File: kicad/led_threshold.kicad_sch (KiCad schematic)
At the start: 14 parts, among them U16 PC817, U19 PC817, U21 OPA189

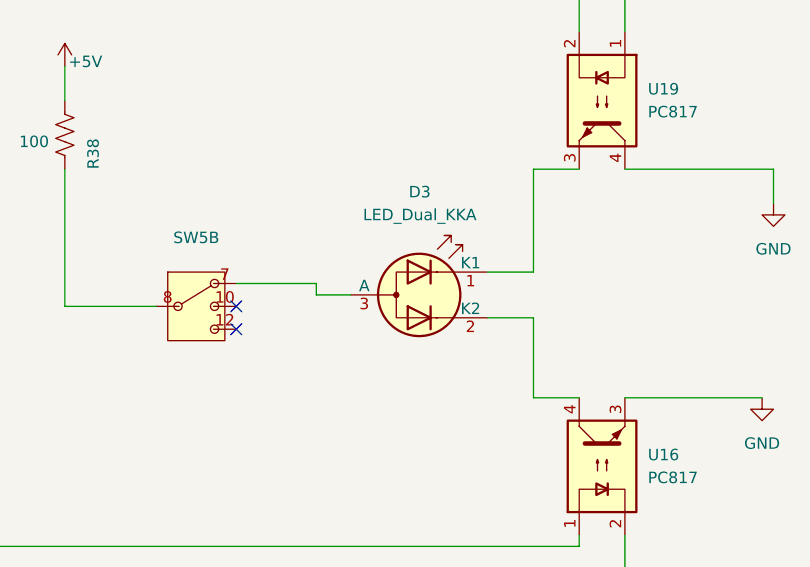
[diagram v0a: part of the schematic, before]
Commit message: Finished Schematic and Assigning Footprint pending Review, TODO: Layout Board
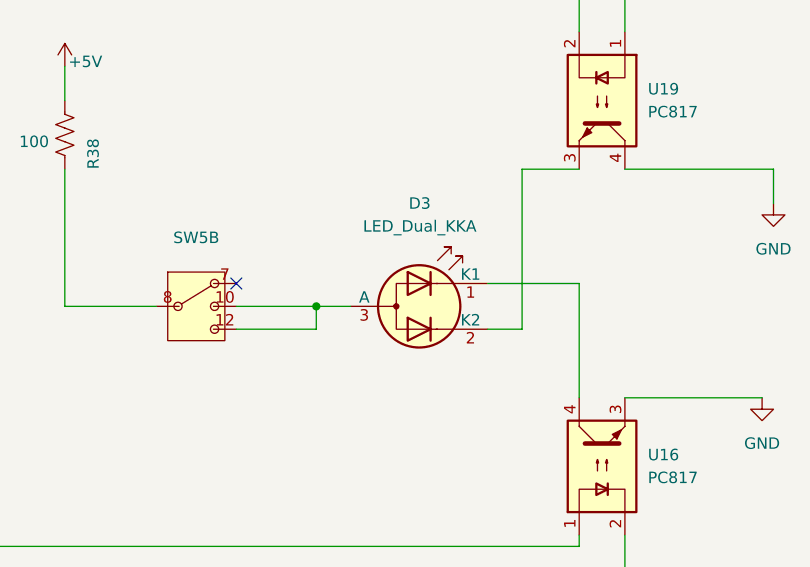
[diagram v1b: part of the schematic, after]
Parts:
- SW5: DIGIKEY (none) -> EG6100-ND; PARTNO (none) -> 1004P6T1B4M7RE
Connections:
- net at U19.3: now also D3.2 (K2); no longer D3.1 (K1)
- net at U16.4: now also D3.1 (K1); no longer D3.2 (K2)
- net at SW5.10: now also D3.3 (A), SW5.12
- net at SW5.7: no longer D3.3 (A)
- no-connect marks 4 -> 3
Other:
- moved on the sheet: D3
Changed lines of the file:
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@@
 	)
 	(junction
+		(at 194.31 66.04)
+		(diameter 0)
+		(color 0 0 0 0)
+	)
+	(junction
 		(at 132.08 116.84)
 		(diameter 0)
@@
 	)
 	(no_connect
-		(at 185.42 66.04)
-	)
-	(no_connect
-		(at 185.42 68.58)
+		(at 185.42 63.5)
 	)
 	(no_connect
@@
 	(wire
 		(pts
+			(xy 213.36 63.5) (xy 223.52 63.5)
+		)
+		(stroke
+			(width 0)
+			(type default)
+		)
+	)
+	(wire
+		(pts
 			(xy 166.37 66.04) (xy 176.53 66.04)
 		)
@@
 	(wire
 		(pts
-			(xy 137.16 105.41) (xy 137.16 106.68)
+			(xy 217.17 50.8) (xy 223.52 50.8)
 		)
 		(stroke
@@
 	(wire
 		(pts
-			(xy 115.57 22.86) (xy 115.57 24.13)
+			(xy 137.16 105.41) (xy 137.16 106.68)
 		)
 		(stroke
@@
 	(wire
 		(pts
-			(xy 93.98 82.55) (xy 87.63 82.55)
+			(xy 115.57 22.86) (xy 115.57 24.13)
 		)
 		(stroke
@@
 	(wire
 		(pts
-			(xy 228.6 19.05) (xy 228.6 17.78)
+			(xy 93.98 82.55) (xy 87.63 82.55)
 		)
 		(stroke
@@
 	(wire
 		(pts
-			(xy 218.44 67.31) (xy 218.44 76.2)
+			(xy 228.6 19.05) (xy 228.6 17.78)
 		)
 		(stroke
@@
 	(wire
 		(pts
-			(xy 44.45 62.23) (xy 44.45 76.2)
+			(xy 194.31 68.58) (xy 194.31 66.04)
 		)
 		(stroke
@@
 	(wire
 		(pts
-			(xy 228.6 26.67) (xy 228.6 35.56)
+			(xy 44.45 62.23) (xy 44.45 76.2)
 		)
 		(stroke
@@
 	(wire
 		(pts
-			(xy 260.35 148.59) (xy 260.35 151.13)
+			(xy 228.6 26.67) (xy 228.6 35.56)
 		)
 		(stroke
@@
 	(wire
 		(pts
-			(xy 194.31 63.5) (xy 194.31 64.77)
+			(xy 260.35 148.59) (xy 260.35 151.13)
 		)
 		(stroke
@@
 	(wire
 		(pts
-			(xy 218.44 50.8) (xy 223.52 50.8)
-		)
-		(stroke
-			(width 0)
-			(type default)
-		)
-	)
-	(wire
-		(pts
 			(xy 81.28 87.63) (xy 93.98 87.63)
 		)
@@
 	(wire
 		(pts
-			(xy 213.36 62.23) (xy 218.44 62.23)
-		)
-		(stroke
-			(width 0)
-			(type default)
-		)
-	)
-	(wire
-		(pts
 			(xy 132.08 123.19) (xy 137.16 123.19)
 		)
@@
 	(wire
 		(pts
-			(xy 218.44 76.2) (xy 223.52 76.2)
-		)
-		(stroke
-			(width 0)
-			(type default)
-		)
-	)
-	(wire
-		(pts
 			(xy 137.16 124.46) (xy 137.16 123.19)
 		)
@@
 	(wire
 		(pts
-			(xy 185.42 63.5) (xy 194.31 63.5)
+			(xy 185.42 66.04) (xy 194.31 66.04)
 		)
 		(stroke
@@
 	(wire
 		(pts
+			(xy 217.17 68.58) (xy 217.17 50.8)
+		)
+		(stroke
+			(width 0)
+			(type default)
+		)
+	)
+	(wire
+		(pts
 			(xy 154.94 31.75) (xy 223.52 31.75)
 		)
@@
 	(wire
 		(pts
-			(xy 194.31 64.77) (xy 198.12 64.77)
+			(xy 194.31 66.04) (xy 198.12 66.04)
 		)
 		(stroke
@@
 	(wire
 		(pts
-			(xy 218.44 62.23) (xy 218.44 50.8)
+			(xy 213.36 68.58) (xy 217.17 68.58)
 		)
 		(stroke
@@
 	(wire
 		(pts
-			(xy 151.13 144.78) (xy 151.13 143.51)
+			(xy 223.52 63.5) (xy 223.52 76.2)
 		)
 		(stroke
@@
 	(wire
 		(pts
-			(xy 213.36 67.31) (xy 218.44 67.31)
+			(xy 151.13 144.78) (xy 151.13 143.51)
 		)
 		(stroke
@@
 	(wire
 		(pts
+			(xy 185.42 68.58) (xy 194.31 68.58)
+		)
+		(stroke
+			(width 0)
+			(type default)
+		)
+	)
+	(wire
+		(pts
 			(xy 132.08 111.76) (xy 132.08 116.84)
 		)
@@
 			)
 		)
+		(property "DIGIKEY" "EG6100-ND"
+			(at 260.35 143.51 0)
+			(effects
+				(font
+					(size 1.27 1.27)
+				)
+				(hide yes)
+			)
+		)
+		(property "PARTNO" "1004P6T1B4M7RE"
+			(at 260.35 143.51 0)
+			(effects
+				(font
+					(size 1.27 1.27)
+				)
+				(hide yes)
+			)
+		)
 		(pin "9"
 		)
@@
 			)
 		)
+		(property "DIGIKEY" "EG6100-ND"
+			(at 180.34 66.04 0)
+			(effects
+				(font
+					(size 1.27 1.27)
+				)
+				(hide yes)
+			)
+		)
+		(property "PARTNO" "1004P6T1B4M7RE"
+			(at 180.34 66.04 0)
+			(effects
+				(font
+					(size 1.27 1.27)
+				)
+				(hide yes)
+			)
+		)
 		(pin "9"
 		)
@@
 	(symbol
 		(lib_id "Device:LED_Dual_KKA")
-		(at 205.74 64.77 0)
+		(at 205.74 66.04 0)
 		(unit 1)
 		(exclude_from_sim no)
@@
 		(fields_autoplaced yes)
 		(property "Reference" "D3"
-			(at 205.8035 53.34 0)
+			(at 205.8035 54.61 0)
 			(effects
 				(font
@@
 		)
 		(property "Value" "LED_Dual_KKA"
-			(at 205.8035 55.88 0)
+			(at 205.8035 57.15 0)
 			(effects
 				(font
@@
 		)
 		(property "Footprint" "Custom_Footprints:GR LED"
-			(at 207.01 64.77 0)
+			(at 207.01 66.04 0)
 			(effects
 				(font
@@
 		)
 		(property "Datasheet" "~"
-			(at 207.01 64.77 0)
+			(at 207.01 66.04 0)
 			(effects
 				(font
@@
 		)
 		(property "Description" "Dual LED, common anode on pin 3"
-			(at 205.74 64.77 0)
+			(at 205.74 66.04 0)
 			(effects
 				(font
@@
 		)
 		(property "DIGIKEY" "160-2033-2-ND"
-			(at 205.74 64.77 0)
+			(at 205.74 66.04 0)
 			(effects
 				(font
@@
 		)
 		(property "PARTNO" "LTST-S326KGJRKT"
-			(at 205.74 64.77 0)
+			(at 205.74 66.04 0)
 			(effects
 				(font

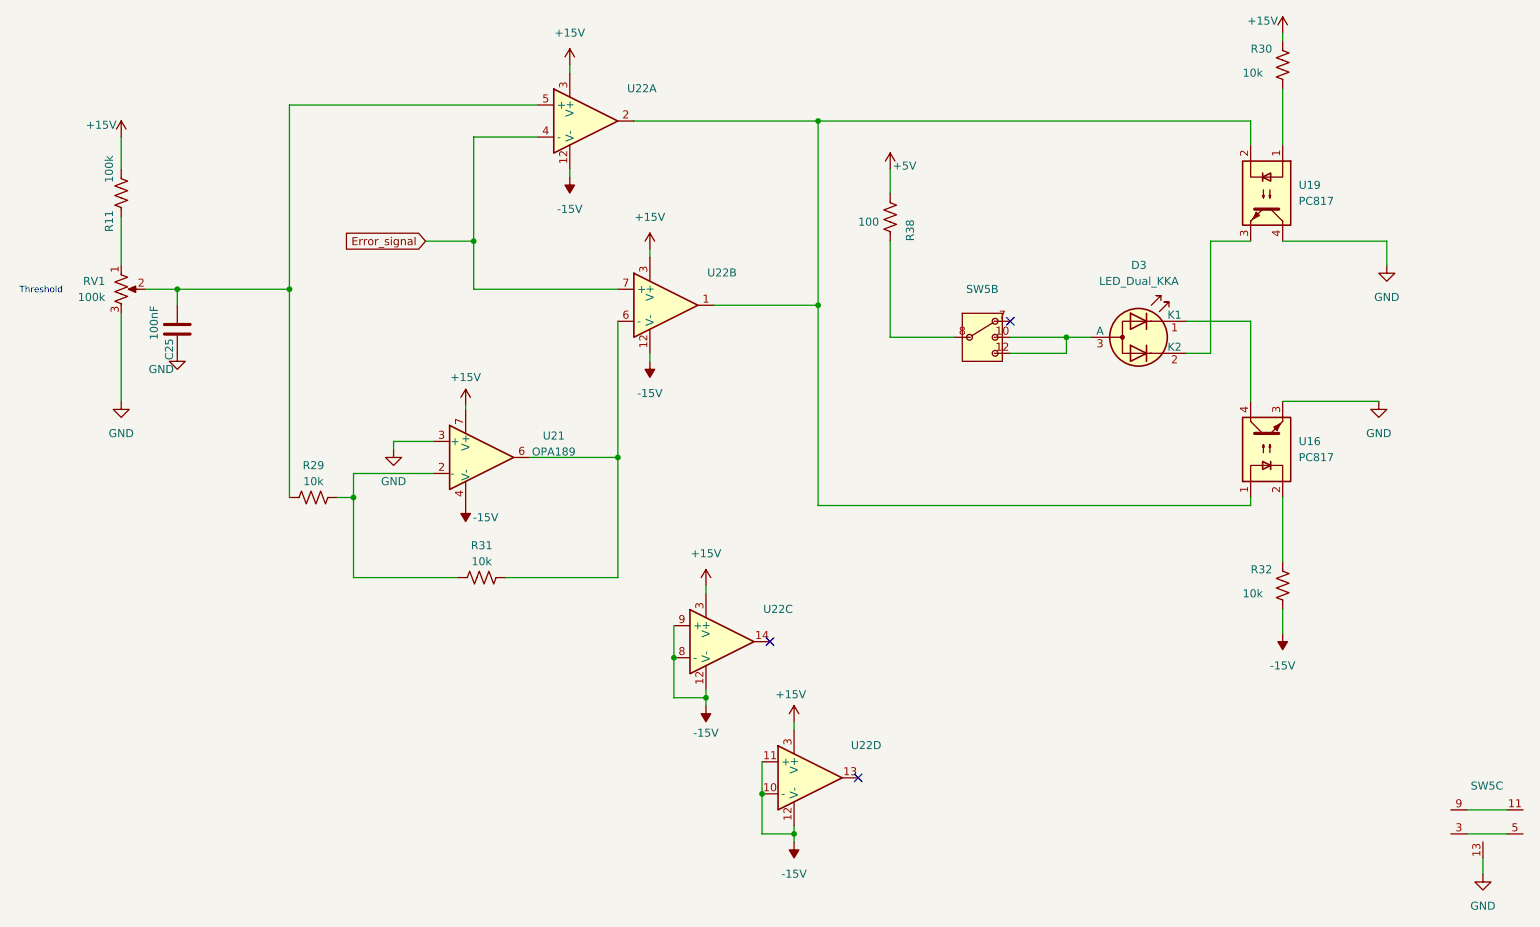
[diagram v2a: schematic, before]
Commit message: Fixed Error Threshold Control, replaced 2x optocouplers with transistors, added power rectification + regulators for 15VAC to +- 15VDC, finished pcb routing, TODO: Check all components have parts, check IC cap filtering, check error threshold schem
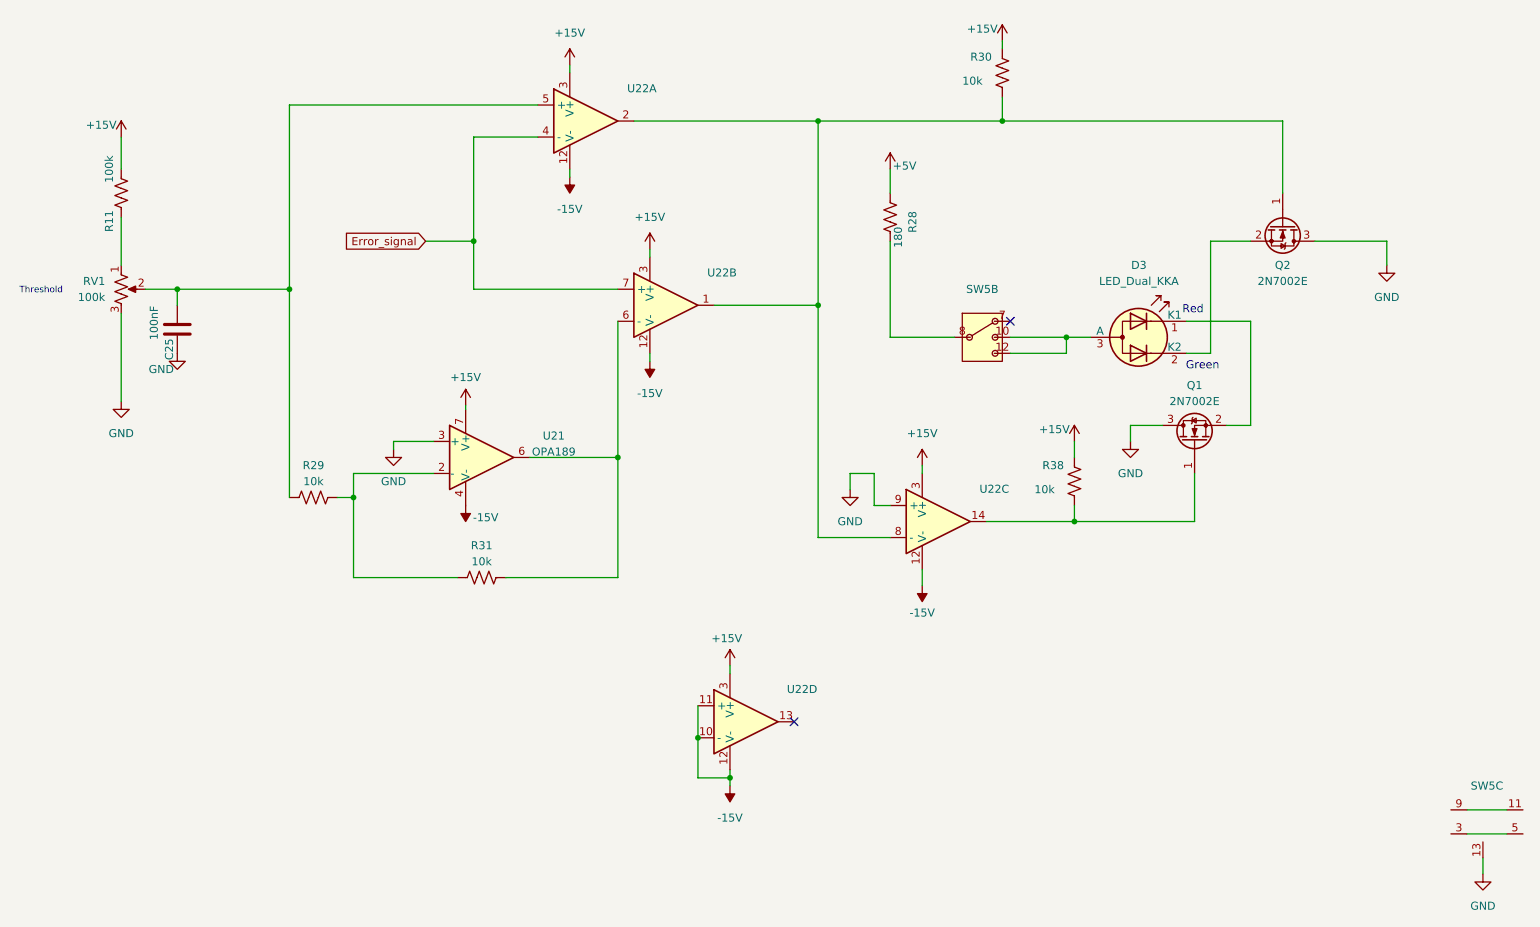
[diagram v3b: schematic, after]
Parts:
- removed R32: 10k, Resistor_SMD:R_0805_2012Metric, symbol Device:R_US
- removed U16, U19: PC817, Package_DIP:DIP-4_W7.62mm, symbol Isolator:PC817
- added Q1, Q2: 2N7002E, Package_TO_SOT_SMD:SOT-23, symbol Transistor_FET:2N7002E
- added R28: 180, Resistor_SMD:R_0805_2012Metric, symbol Device:R_US
- R38: value 100 -> 10k
- U22: DIGIKEY (none) -> UPC177G2(20)-E2-A; MOUSER (none) -> 968-UPC177G220-E2A; PARTNO (none) -> UPC177G2(20)-E2-A
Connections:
- net +15V: now also R38.2
- net +5V: now also R28.1; no longer R38.2
- net -15V: no longer U22.8 (-), U22.9 (+)
- net GND: now also U22.9 (+), Q1.3 (D), Q2.3 (D)
- net at U22.1, U22.2: now also R30.1, U22.8 (-), Q2.1 (G)
- net at D3.2 (K2): now also Q2.2 (S)
- net at R38.1: now also U22.14, Q1.1 (G); no longer SW5.8
- net at D3.1 (K1): now also Q1.2 (S)
- new net: R28.2, SW5.8
- no-connect marks 3 -> 2
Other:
- note added: "Green"
- note added: "Red"
- moved on the sheet: R30, U22C, U22D

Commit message: Fixed LED Threshold schematic, added second power input screw terminal, first attempt at final placement and routing
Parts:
- R30, R38: DIGIKEY (none) -> 2019-RN73H2ATTD1002B25CT-ND
- RV1: DIGIKEY (none) -> 118-PV36W104C01B00-ND; PARTNO (none) -> PV36W104C01B00
- SW5: value ~ -> EG6100-ND
- U22: value ~ -> 4x Comparator
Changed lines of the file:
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@@
+			)
+		)
+		(property "MPN" ""
+			(at 195.58 88.9 0)
+			(effects
+				(font
+					(size 1.27 1.27)
+				)
+				(hide yes)
+			)
+		)
+		(property "DIGIKEY" "2019-RN73H2ATTD1002B25CT-ND"
+			(at 195.58 88.9 0)
+			(effects
+				(font
+					(size 1.27 1.27)
+				)
+				(hide yes)
 			)
 		)
@@
 			)
 		)
+		(property "MPN" ""
+			(at 74.93 91.44 90)
+			(effects
+				(font
+					(size 1.27 1.27)
+				)
+				(hide yes)
+			)
+		)
 		(pin "1"
 		)
@@
 			)
 		)
-		(property "Value" "~"
+		(property "Value" "4x Comparator"
 			(at 139.7 57.7149 0)
 			(effects
@@
 		)
 		(property "PARTNO" "UPC177G2(20)-E2-A"
+			(at 129.54 60.96 0)
+			(effects
+				(font
+					(size 1.27 1.27)
+				)
+				(hide yes)
+			)
+		)
+		(property "MPN" ""
 			(at 129.54 60.96 0)
 			(effects
@@
 			)
 		)
+		(property "MPN" ""
+			(at 184.15 24.13 0)
+			(effects
+				(font
+					(size 1.27 1.27)
+				)
+				(hide yes)
+			)
+		)
+		(property "DIGIKEY" "2019-RN73H2ATTD1002B25CT-ND"
+			(at 184.15 24.13 0)
+			(effects
+				(font
+					(size 1.27 1.27)
+				)
+				(hide yes)
+			)
+		)
 		(pin "1"
 		)
@@
 			)
 		)
+		(property "MPN" ""
+			(at 228.6 48.26 90)
+			(effects
+				(font
+					(size 1.27 1.27)
+				)
+				(hide yes)
+			)
+		)
 		(pin "3"
 		)
@@
 			)
 		)
+		(property "MPN" ""
+			(at 44.45 43.18 90)
+			(effects
+				(font
+					(size 1.27 1.27)
+				)
+				(hide yes)
+			)
+		)
 		(pin "1"
 		)
@@
 			)
 		)
+		(property "MPN" ""
+			(at 101.6 104.14 90)
+			(effects
+				(font
+					(size 1.27 1.27)
+				)
+				(hide yes)
+			)
+		)
 		(pin "1"
 		)
@@
 			)
 		)
+		(property "MPN" ""
+			(at 101.6 85.09 0)
+			(effects
+				(font
+					(size 1.27 1.27)
+				)
+				(hide yes)
+			)
+		)
 		(pin "1"
 		)
@@
 			)
 		)
-		(property "Value" "~"
+		(property "Value" "EG6100-ND"
 			(at 260.985 139.7 0)
 			(effects
@@
 		)
 		(property "PARTNO" "1004P6T1B4M7RE"
+			(at 260.35 143.51 0)
+			(effects
+				(font
+					(size 1.27 1.27)
+				)
+				(hide yes)
+			)
+		)
+		(property "MPN" ""
 			(at 260.35 143.51 0)
 			(effects
@@
 			)
 		)
-		(property "Value" "~"
+		(property "Value" "4x Comparator"
 			(at 182.88 92.0049 0)
 			(effects
@@
 		)
 		(property "PARTNO" "UPC177G2(20)-E2-A"
+			(at 172.72 95.25 0)
+			(effects
+				(font
+					(size 1.27 1.27)
+				)
+				(hide yes)
+			)
+		)
+		(property "MPN" ""
 			(at 172.72 95.25 0)
 			(effects
@@
 			)
 		)
+		(property "DIGIKEY" "118-PV36W104C01B00-ND"
+			(at 44.45 58.42 0)
+			(effects
+				(font
+					(size 1.27 1.27)
+				)
+				(hide yes)
+			)
+		)
+		(property "PARTNO" "PV36W104C01B00"
+			(at 44.45 58.42 0)
+			(effects
+				(font
+					(size 1.27 1.27)
+				)
+				(hide yes)
+			)
+		)
 		(pin "2"
 		)
@@
 			)
 		)
-		(property "Value" "~"
+		(property "Value" "4x Comparator"
 			(at 152.4 123.7549 0)
 			(effects
@@
 		)
 		(property "PARTNO" "UPC177G2(20)-E2-A"
+			(at 142.24 127 0)
+			(effects
+				(font
+					(size 1.27 1.27)
+				)
+				(hide yes)
+			)
+		)
+		(property "MPN" ""
 			(at 142.24 127 0)
 			(effects
@@
 			)
 		)
-		(property "Value" "~"
+		(property "Value" "EG6100-ND"
 			(at 180.975 60.96 0)
 			(effects
@@
 		)
 		(property "PARTNO" "1004P6T1B4M7RE"
+			(at 180.34 66.04 0)
+			(effects
+				(font
+					(size 1.27 1.27)
+				)
+				(hide yes)
+			)
+		)
+		(property "MPN" ""
 			(at 180.34 66.04 0)
 			(effects
@@
 			)
 		)
+		(property "MPN" ""
+			(at 166.37 46.99 90)
+			(effects
+				(font
+					(size 1.27 1.27)
+				)
+				(hide yes)
+			)
+		)
 		(pin "1"
 		)
@@
 			)
 		)
+		(property "MPN" ""
+			(at 205.74 66.04 0)
+			(effects
+				(font
+					(size 1.27 1.27)
+				)
+				(hide yes)
+			)
+		)
 		(pin "1"
 		)
@@
 		(property "Description" ""
 			(at 53.34 64.77 0)
+			(effects
+				(font
+					(size 1.27 1.27)
+				)
+				(hide yes)
+			)
+		)
+		(property "MPN" ""
+			(at 53.34 64.77 90)
 			(effects
 				(font
@@
 			)
 		)
-		(property "Value" "~"
+		(property "Value" "4x Comparator"
 			(at 127 28.5049 0)
 			(effects
@@
 			(at 116.84 31.75 0)
 			(effects
+				(font
+					(size 1.27 1.27)
+				)
+				(hide yes)
+			)
+		)
+		(property "MPN" ""
+			(at 116.84 31.75 0)
+			(effects

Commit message: Removed large cap and rectifier, added transistor resistors
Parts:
- added R32, R39: 100, Resistor_SMD:R_0805_2012Metric, symbol Device:R_US
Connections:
- net at R38.1, U22.14: now also R32.2; no longer Q1.1 (G)
- net at R30.1, U22.1, U22.2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: now also R39.1; no longer Q2.1 (G)
- new net: Q2.1 (G), R39.2
- new net: Q1.1 (G), R32.1
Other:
- moved on the sheet: R38, U22C

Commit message: Condensed Layout, Removed 5V supply, Shortened Board
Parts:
- R28: value 180 -> 1k; DIGIKEY YAG3766CT-ND -> (none); PARTNO AC0805JR-071ML -> (none)
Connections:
- net +5V is gone; now on net +15V: R28.1
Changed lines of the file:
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@@
-	)
-	(symbol
-		(lib_id "power:+5V")
-		(at 166.37 39.37 0)
-		(unit 1)
-		(exclude_from_sim no)
-		(in_bom yes)
-		(on_board yes)
-		(dnp no)
-		(property "Reference" "#PWR074"
-			(at 166.37 43.18 0)
-			(effects
-				(font
-					(size 1.27 1.27)
-				)
-				(hide yes)
-			)
-		)
-		(property "Value" "+5V"
-			(at 168.656 38.862 0)
-			(effects
-				(font
-					(size 1.27 1.27)
-				)
-			)
-		)
-		(property "Footprint" ""
-			(at 166.37 39.37 0)
-			(effects
-				(font
-					(size 1.27 1.27)
-				)
-				(hide yes)
-			)
-		)
-		(property "Datasheet" ""
-			(at 166.37 39.37 0)
-			(effects
-				(font
-					(size 1.27 1.27)
-				)
-				(hide yes)
-			)
-		)
-		(property "Description" "Power symbol creates a global label with name \"+5V\""
-			(at 166.37 39.37 0)
-			(effects
-				(font
-					(size 1.27 1.27)
-				)
-				(hide yes)
-			)
-		)
-		(pin "1"
-		)
-		(instances
-			(project "intensity_pi"
-				(path "/3a3d7bcb-6fa5-41ef-9ea1-6d4ab7c492fd/0e4e37c0-2fc7-4de2-ba74-9d178da3762c"
-					(reference "#PWR074")
-					(unit 1)
-				)
-			)
-		)
 	)
 	(symbol
@@
 			)
 		)
-		(property "Value" "180"
+		(property "Value" "1k"
 			(at 167.64 50.165 90)
 			(effects
@@
 			)
 		)
-		(property "DIGIKEY" "YAG3766CT-ND"
+		(property "DIGIKEY" ""
 			(at 166.37 46.99 90)
 			(effects
@@
 			)
 		)
-		(property "PARTNO" "AC0805JR-071ML"
+		(property "PARTNO" ""
 			(at 166.37 46.99 90)
 			(effects
@@
 					(unit 1)
 				)
+			)
+		)
+	)
+	(symbol
+		(lib_id "power:+15V")
+		(at 166.37 39.37 0)
+		(unit 1)
+		(exclude_from_sim no)
+		(in_bom yes)
+		(on_board yes)
+		(dnp no)
+		(fields_autoplaced yes)
+		(property "Reference" "#PWR074"
+			(at 166.37 43.18 0)
+			(effects
+				(font
+					(size 1.27 1.27)
+				)
+				(hide yes)
+			)
+		)
+		(property "Value" "+15V"
+			(at 166.37 34.29 0)
+			(effects
+				(font
+					(size 1.27 1.27)
+				)
+			)
+		)
+		(property "Footprint" ""
+			(at 166.37 39.37 0)
+			(effects
+				(font
+					(size 1.27 1.27)
+				)
+				(hide yes)
+			)
+		)
+		(property "Datasheet" ""
+			(at 166.37 39.37 0)
+			(effects
+				(font
+					(size 1.27 1.27)
+				)
+				(hide yes)
+			)
+		)
+		(property "Description" "Power symbol creates a global label with name \"+15V\""
+			(at 166.37 39.37 0)
+			(effects
+				(font
+					(size 1.27 1.27)
+				)
+				(hide yes)
+			)
+		)
+		(pin "1"
+		)
+		(instances
+			(project ""
+				(path "/3a3d7bcb-6fa5-41ef-9ea1-6d4ab7c492fd/0e4e37c0-2fc7-4de2-ba74-9d178da3762c"
+					(reference "#PWR074")
+					(unit 1)
+				)
